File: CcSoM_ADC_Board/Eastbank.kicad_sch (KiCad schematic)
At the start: 1 part, among them J1 SoM Connector

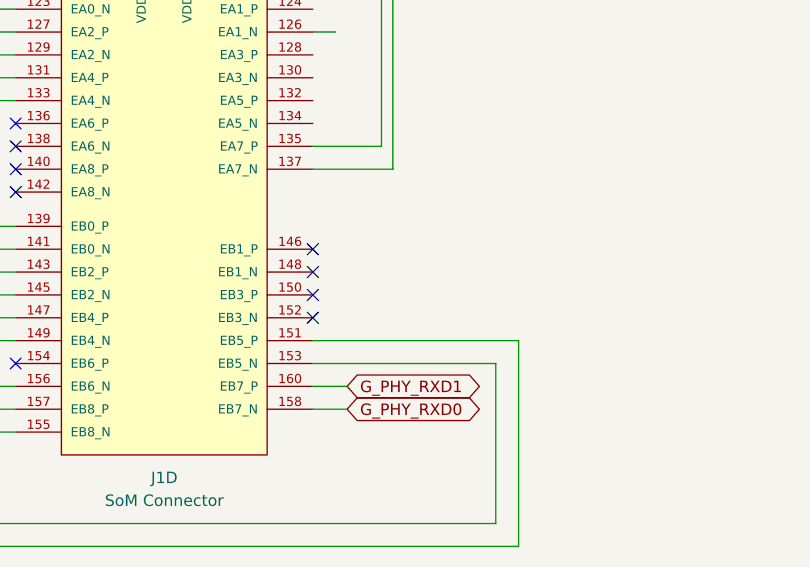
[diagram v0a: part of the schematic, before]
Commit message: changed from 10Bit ADC to 12Bit
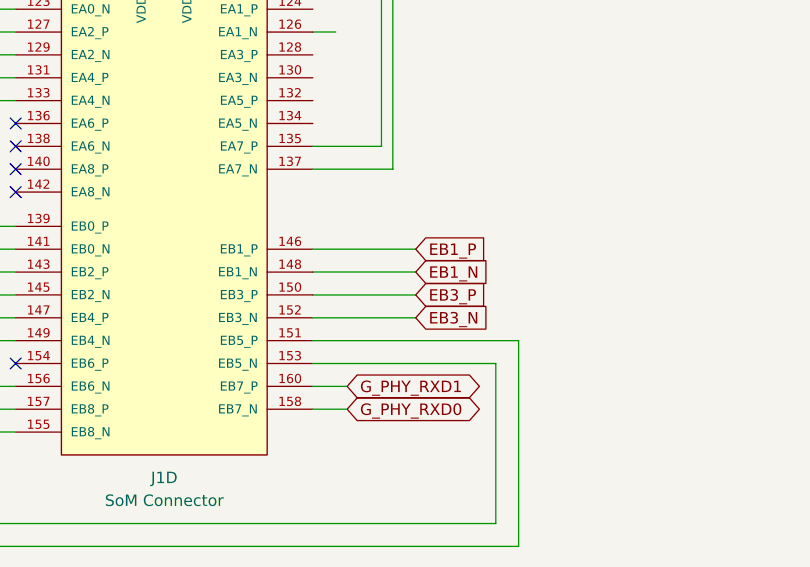
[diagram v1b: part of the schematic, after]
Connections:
- net EB1_P: now reaches J1.146 (EB1_P)
- net EB1_N: now reaches J1.148 (EB1_N)
- net EB3_P: now reaches J1.150 (EB3_P)
- net EB3_N: now reaches J1.152 (EB3_N)
- no-connect marks 9 -> 5
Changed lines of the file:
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@@
-	)
-	(no_connect
-		(at 157.48 102.87)
-	)
-	(no_connect
-		(at 157.48 100.33)
-	)
-	(no_connect
-		(at 157.48 97.79)
 	)
 	(no_connect
@@
 	)
 	(no_connect
-		(at 157.48 105.41)
-	)
-	(no_connect
 		(at 124.46 91.44)
 	)
@@
 	(wire
 		(pts
+			(xy 157.48 97.79) (xy 168.91 97.79)
+		)
+		(stroke
+			(width 0)
+			(type default)
+		)
+	)
+	(wire
+		(pts
 			(xy 166.37 63.5) (xy 166.37 88.9)
 		)
@@
 	(wire
 		(pts
+			(xy 157.48 102.87) (xy 168.91 102.87)
+		)
+		(stroke
+			(width 0)
+			(type default)
+		)
+	)
+	(wire
+		(pts
 			(xy 165.1 86.36) (xy 157.48 86.36)
 		)
@@
 	(wire
 		(pts
+			(xy 157.48 105.41) (xy 168.91 105.41)
+		)
+		(stroke
+			(width 0)
+			(type default)
+		)
+	)
+	(wire
+		(pts
 			(xy 91.44 113.03) (xy 101.6 113.03)
 		)
@@
 		(pts
 			(xy 88.9 78.74) (xy 124.46 78.74)
+		)
+		(stroke
+			(width 0)
+			(type default)
+		)
+	)
+	(wire
+		(pts
+			(xy 157.48 100.33) (xy 168.91 100.33)
 		)
 		(stroke
@@
 			)
 			(justify left bottom)
+		)
+	)
+	(global_label "EB3_P"
+		(shape input)
+		(at 168.91 102.87 0)
+		(fields_autoplaced yes)
+		(effects
+			(font
+				(size 1.27 1.27)
+			)
+			(justify left)
+		)
+		(property "Intersheetrefs" "${INTERSHEET_REFS}"
+			(at 177.7613 102.87 0)
+			(effects
+				(font
+					(size 1.27 1.27)
+				)
+				(justify left)
+				(hide yes)
+			)
 		)
 	)
@@
 		)
 	)
+	(global_label "EB1_N"
+		(shape input)
+		(at 168.91 100.33 0)
+		(fields_autoplaced yes)
+		(effects
+			(font
+				(size 1.27 1.27)
+			)
+			(justify left)
+		)
+		(property "Intersheetrefs" "${INTERSHEET_REFS}"
+			(at 177.8218 100.33 0)
+			(effects
+				(font
+					(size 1.27 1.27)
+				)
+				(justify left)
+				(hide yes)
+			)
+		)
+	)
 	(global_label "{EB_even}"
 		(shape input)
@@
 		)
 	)
+	(global_label "EB3_N"
+		(shape input)
+		(at 168.91 105.41 0)
+		(fields_autoplaced yes)
+		(effects
+			(font
+				(size 1.27 1.27)
+			)
+			(justify left)
+		)
+		(property "Intersheetrefs" "${INTERSHEET_REFS}"
+			(at 177.8218 105.41 0)
+			(effects
+				(font
+					(size 1.27 1.27)
+				)
+				(justify left)
+				(hide yes)
+			)
+		)
+	)
 	(global_label "G_PHY_RXD0"
 		(shape bidirectional)
@@
 				(hide yes)
 			)
+		)
+	)
+	(global_label "EB1_P"
+		(shape input)
+		(at 168.91 97.79 0)
+		(fields_autoplaced yes)
+		(effects
+			(font
+				(size 1.27 1.27)
+			)
+			(justify left)
+		)
+		(property "Intersheetrefs" "${INTERSHEET_REFS}"
+			(at 177.7613 97.79 0)
+			(effects
+				(font
+					(size 1.27 1.27)
+				)
+				(justify left)
+				(hide yes)
+			)

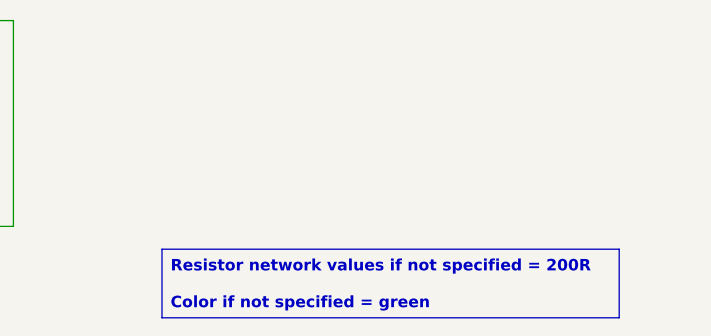
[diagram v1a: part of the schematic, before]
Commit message: corrected schematic created pdf and bom file
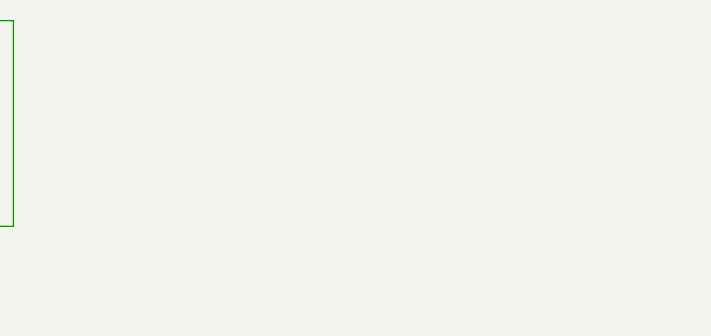
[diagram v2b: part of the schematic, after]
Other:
- title: SoM Programmer & Tester -> SoM Programmer & ADC Board
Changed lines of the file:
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@@
 	(paper "A4")
 	(title_block
-		(title "SoM Programmer & Tester")
-		(date "2024-12-20")
+		(title "SoM Programmer & ADC Board")
+		(date "2026-02-09")
 		(rev "0.1")
 		(company "Technische Hochschule Köln")
 		(comment 1 "Felix Sebastian Nitz")
-	)
-	(text_box "Resistor network values if not specified = 200R\n\nColor if not specified = green"
-		(exclude_from_sim no)
-		(at 196.85 133.35 0)
-		(size 50.8 7.62)
-		(margins 0.9525 0.9525 0.9525 0.9525)
-		(stroke
-			(width 0)
-			(type default)
-		)
-		(fill
-			(type none)
-		)
-		(effects
-			(font
-				(size 1.27 1.27)
-				(thickness 0.254)
-				(bold yes)
-			)
-			(justify left)
-		)
+		(comment 2 "Ismail Özdemirkan")
 	)
 	(no_connect

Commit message: last before rotating adc
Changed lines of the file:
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@@
+	(wire
+		(pts
+			(xy 157.48 83.82) (xy 161.29 83.82)
+		)
+		(stroke
+			(width 0)
+			(type default)
+		)
+	)
 	(wire
 		(pts
@@
 		)
 		(stroke
+			(width 0)
+			(type default)
+		)
+	)
+	(wire
+		(pts
+			(xy 157.48 81.28) (xy 161.29 81.28)
+		)
+		(stroke

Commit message: digikey no not complete
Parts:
- J1: DigiKey_no (none) -> A121565-ND
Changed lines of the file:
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@@
+			)
+		)
+		(property "DigiKey_no" "A121565-ND"
+			(at 140.97 83.82 0)
+			(effects
+				(font
+					(size 1.27 1.27)
+				)
+				(hide yes)
 			)
 		)
